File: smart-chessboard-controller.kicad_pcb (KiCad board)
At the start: 4 copper layers, 89.8 x 92.5 mm, 71 parts, among them J1 USB_C_Receptacle_USB2.0, J2 Micro_SD_Card_Det_Hirose_DM3C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, J3 Conn_02x03_Odd_Even, J4 Conn_01x12_MountingPin, J5 NX3224T024, J6 Conn_01x05, J7 Conn_01x05, J8 Conn_01x05, J9 Conn_01x05, Q1 S8050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

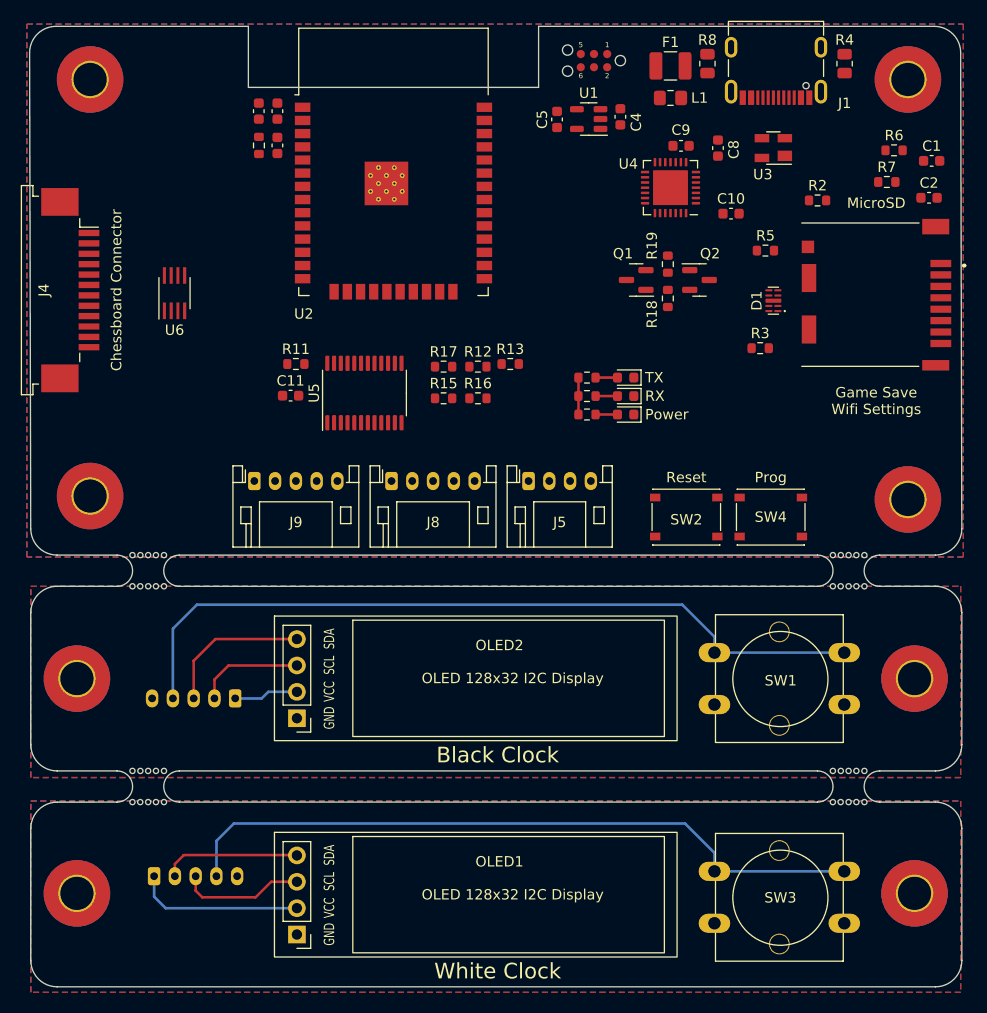
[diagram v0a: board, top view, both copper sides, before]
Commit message: change mounting hole size
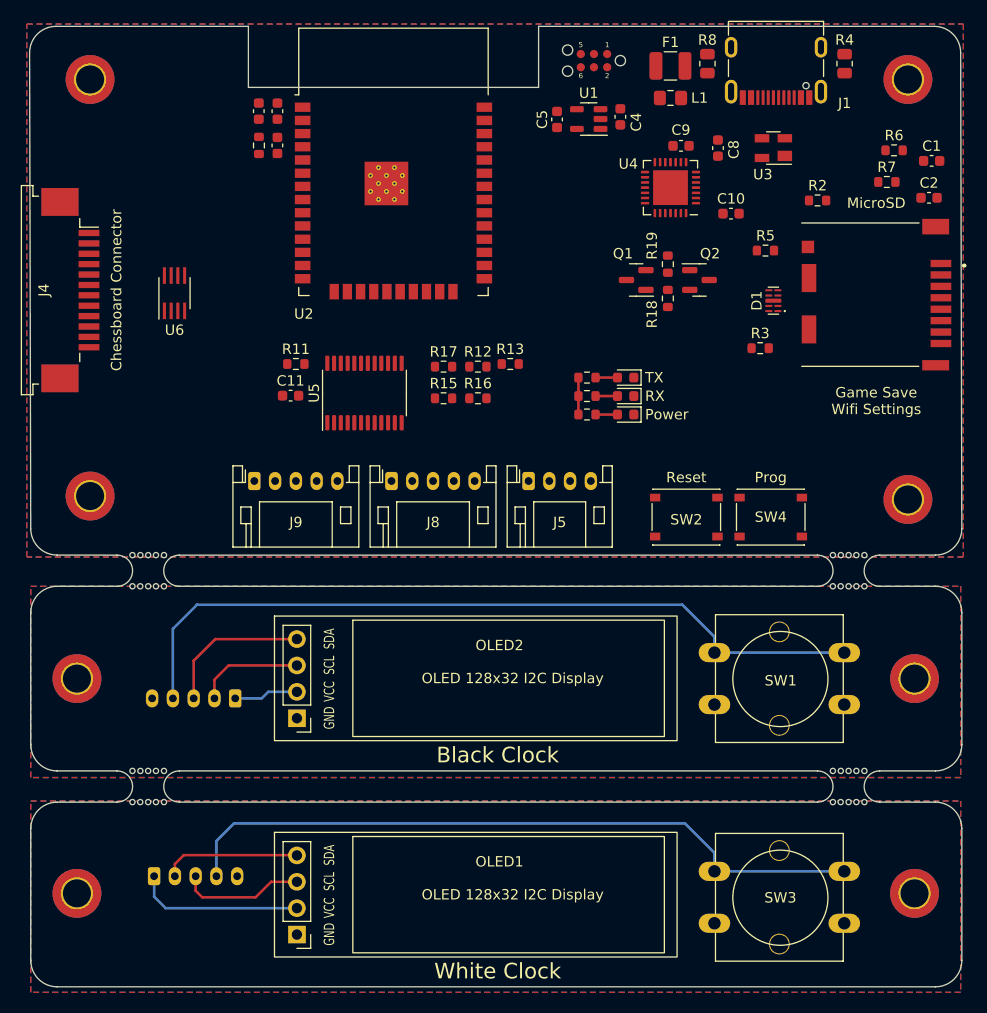
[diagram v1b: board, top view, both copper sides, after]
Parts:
- H1, H2, H3, H4, H5, H6, H7, H8: footprint MountingHole:MountingHole_3.2mm_M3_Pad_TopBottom -> MountingHole:MountingHole_2.7mm_M2.5_DIN965_Pad_TopBottom

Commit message: add some traces
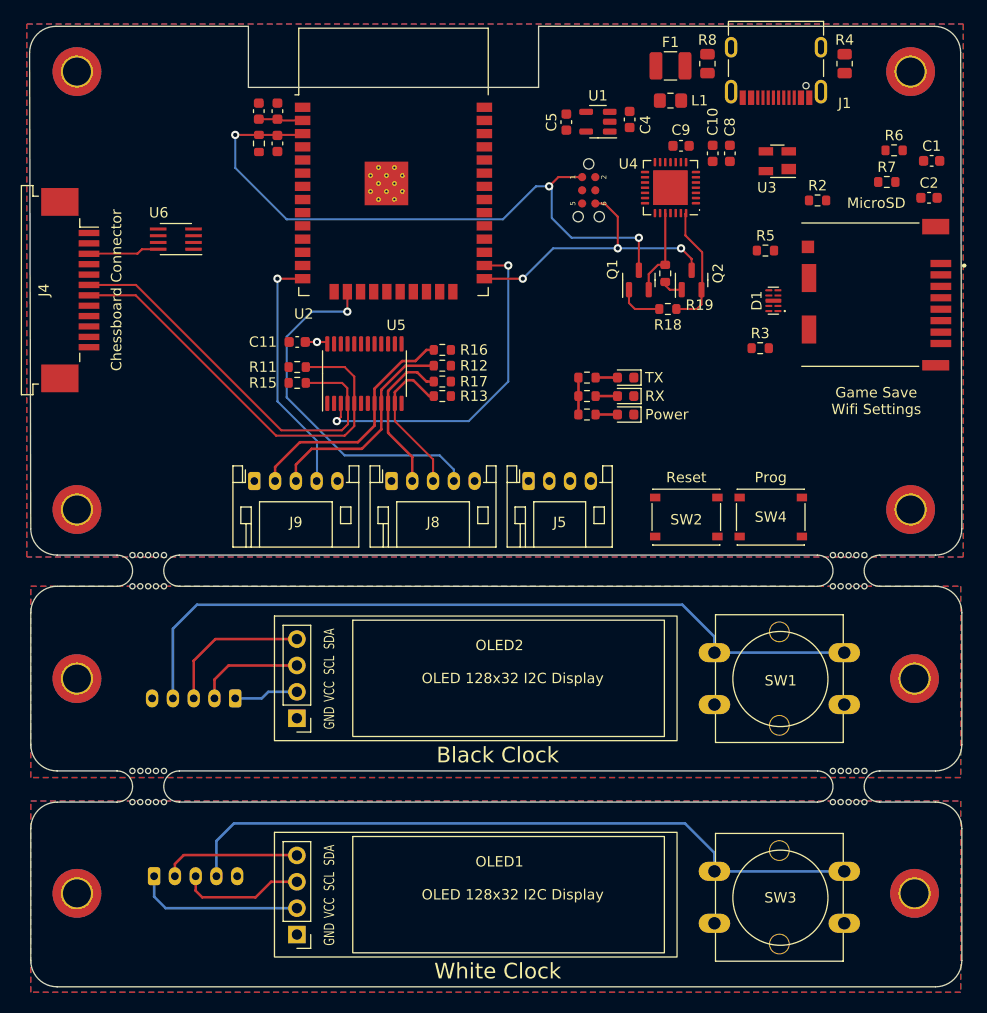
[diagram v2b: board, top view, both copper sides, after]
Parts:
- moved R15 14.2 mm to (99.4, 87.6)
- moved J3 12.5 mm to (127.5, 69.1), turned to -90 degrees
- moved R13 7.23 mm to (113.4, 88.9), turned to 180 degrees
- moved C10 6.07 mm to (139.4, 65.5), turned to 90 degrees
- moved R16 5.79 mm to (113.4, 84.5), turned to 180 degrees
- moved U6 5.21 mm to (87.8, 73.8), turned to 180 degrees
- moved C11 5.21 mm to (99.4, 83.7), turned to 180 degrees
- moved R12 3.43 mm to (113.4, 86.0), turned to 180 degrees
- moved U5 1.87 mm to (105.9, 86.7)
- moved H8 1.81 mm to (78.2, 99.8)
- moved H5 1.48 mm to (78.2, 57.7)
- moved R17 1.44 mm to (113.4, 87.5), turned to 180 degrees
- moved U3 1.33 mm to (145.7, 66.3)
- moved C8 1.25 mm to (141.1, 65.5)
- moved R18 1.02 mm to (135.1, 80.5), turned to 0 degrees
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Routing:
- net /EN: track 0.00 -> 62.7 mm, vias 0 -> 3
- net ~{SCL_IOMUX}: track 0.00 -> 41.3 mm
- net ~{SDA_IOMUX}: track 0.00 -> 38.7 mm
- net /W_MOVE: track 0.00 -> 34.7 mm, vias 0 -> 1
- net /~{I2C_RESET}: track 0.00 -> 33.4 mm, vias 0 -> 2
- net /IO0: track 0.00 -> 28.4 mm, vias 0 -> 3
- net /B_MOVE: track 0.00 -> 23.5 mm, vias 0 -> 1
- net /SCL_DBC: track 0.00 -> 23.4 mm
- net /SDA_DBC: track 0.00 -> 21.0 mm
- net /SDA_DWC: track 0.00 -> 15.1 mm
- net /SCL_DWC: track 0.00 -> 14.9 mm
- net /DTR: track 0.00 -> 12.1 mm
- net /RTS: track 0.00 -> 8.45 mm
- net /LED_IC_5: track 0.00 -> 6.84 mm
- net 3V3: track 25.9 -> 32.4 mm, vias 0 -> 1
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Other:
- board text added: "."

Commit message: add all traces and power traces
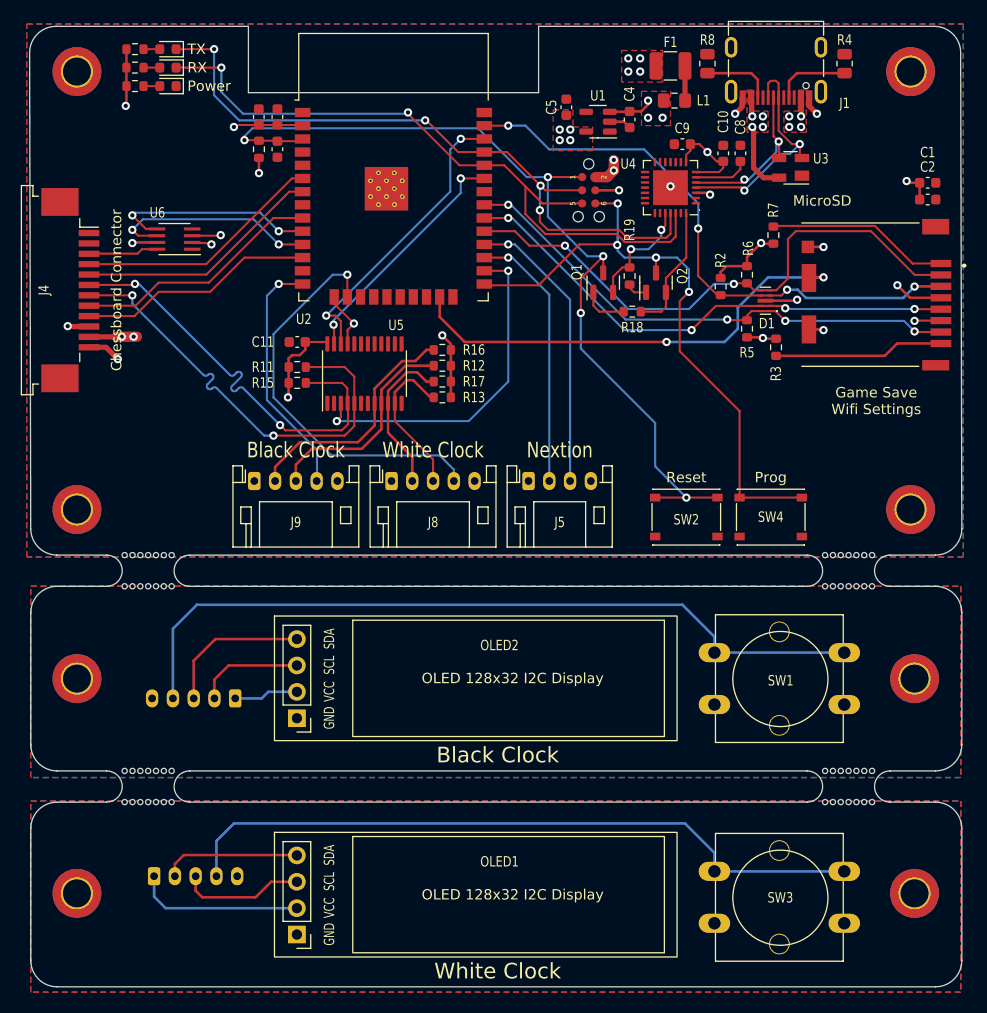
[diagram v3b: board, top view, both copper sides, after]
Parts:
- moved LED2 54.2 mm to (87.0, 57.3)
- moved LED1 54.2 mm to (87.0, 55.5)
- moved LED3 54.2 mm to (87.0, 59.1)
- moved R10 53.8 mm to (83.8, 57.3)
- moved R14 53.8 mm to (83.8, 59.1)
- moved R9 53.8 mm to (83.8, 55.5)
- moved R6 18.5 mm to (142.7, 77.2), turned to 90 degrees
- moved R2 12.5 mm to (140.2, 78.4), turned to 90 degrees
- moved R7 12.1 mm to (145.3, 73.4), turned to -90 degrees
- moved R5 7.74 mm to (142.7, 82.4), turned to -90 degrees
- moved R19 3.44 mm to (131.4, 77.3)
- moved Q1 3.44 mm to (128.9, 78.0)
- moved R18 3.44 mm to (131.7, 80.8)
- moved Q2 3.44 mm to (134.0, 78.0)
- moved C1 2.14 mm to (160.1, 68.4)
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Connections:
- U2 pad 10: /SD_SS -> /LED_IC_3
- U2 pad 11: /LED_IC_3 -> /VLS_EN
- U2 pad 29: /VLS_EN -> /SD_SS
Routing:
- net 3V3: track 32.4 -> 296.2 mm, vias 1 -> 15
- net 5V: track 0.00 -> 124.4 mm, vias 0 -> 7
- net /ESP_RX: track 0.00 -> 66.8 mm, vias 0 -> 2
- net /ESP_TX: track 0.00 -> 66.2 mm, vias 0 -> 4
- net /SD_MOSI: track 0.00 -> 55.8 mm, vias 0 -> 4
- net /SD_SS: track 0.00 -> 54.7 mm, vias 0 -> 2
- net /SD_MISO: track 0.00 -> 50.0 mm, vias 0 -> 4
- net /SD_SCK: track 0.00 -> 49.5 mm, vias 0 -> 4
- net /SD_DET: track 0.00 -> 45.1 mm, vias 0 -> 2
- net VBUS: track 0.00 -> 43.5 mm, vias 0 -> 14
- net /IO0: track 28.4 -> 61.8 mm, vias 3 -> 4
- net /~{I2C_SCL}: track 0.00 -> 28.5 mm, vias 0 -> 2
- net /TX2: track 0.00 -> 27.9 mm, vias 0 -> 1
- net GND: track 0.23 -> 27.7 mm, vias 0 -> 12
- net /RX2: track 0.00 -> 25.7 mm, vias 0 -> 1
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- added copper zone on F.Cu, net 3V3
- added copper zone on In1.Cu, net 3V3
- added copper zone on F.Cu, net 5V
- added copper zone on In1.Cu, net GND
- added copper zone on In2.Cu, net GND
- added copper zone on F.Cu, net VBUS
- added copper zone on In1.Cu, net VBUS
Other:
- outline, holes or cut-outs redrawn
- board text added: "Nextion"

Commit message: add logos and fix DRC issues
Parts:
- added REF**: KiCad-Logo2_6mm_SilkScreen, Symbol:KiCad-Logo2_6mm_SilkScreen, F.Cu at (134.1, 87.9)
- added REF**: OSHW-Logo2_9.8x8mm_SilkScreen, Symbol:OSHW-Logo2_9.8x8mm_SilkScreen, F.Cu at (85.3, 93.9)
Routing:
- net /D_N: track 16.1 -> 25.1 mm, vias 2 -> 3
- net 5V: track 124.4 -> 127.7 mm
- net 3V3: track 296.2 -> 294.9 mm
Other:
- board text added: "${COMPANY} ${TITLE} Rev ${REVISION} / ${ISSUE_DATE}"

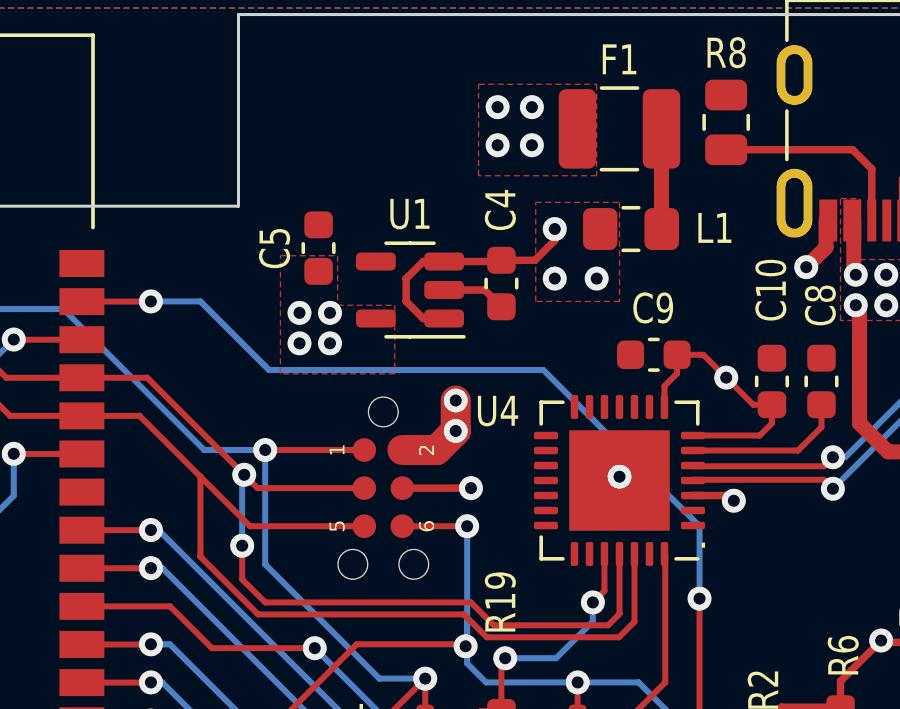
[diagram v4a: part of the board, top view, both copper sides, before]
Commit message: refactor LDO layout
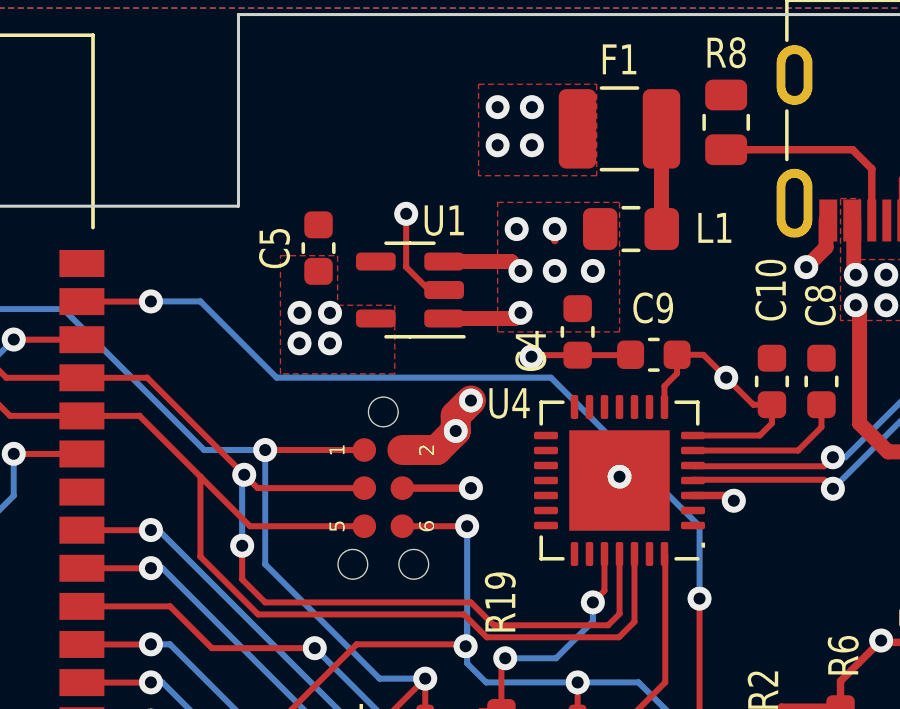
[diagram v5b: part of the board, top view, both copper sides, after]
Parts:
- moved C4 3.01 mm to (134.0, 63.9)
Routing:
- net 5V: track 127.7 -> 122.4 mm, vias 7 -> 10
- net GND: track 27.7 -> 32.2 mm, vias 12 -> 14
- added copper zone on In2.Cu, net 5V

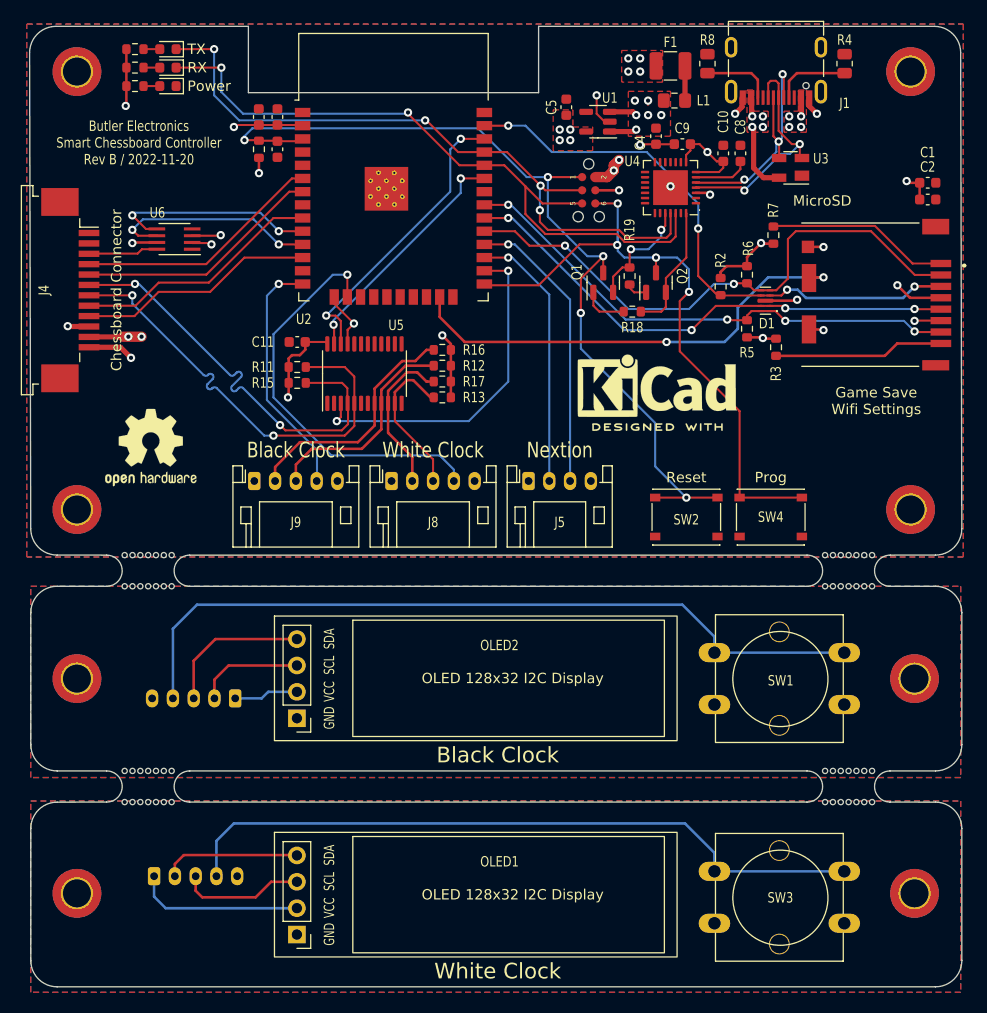
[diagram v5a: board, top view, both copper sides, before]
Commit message: move usb-c to the side of the pcb
- revise ground nets for clock boards
- add backup led IC data line if the voltage regulator fails
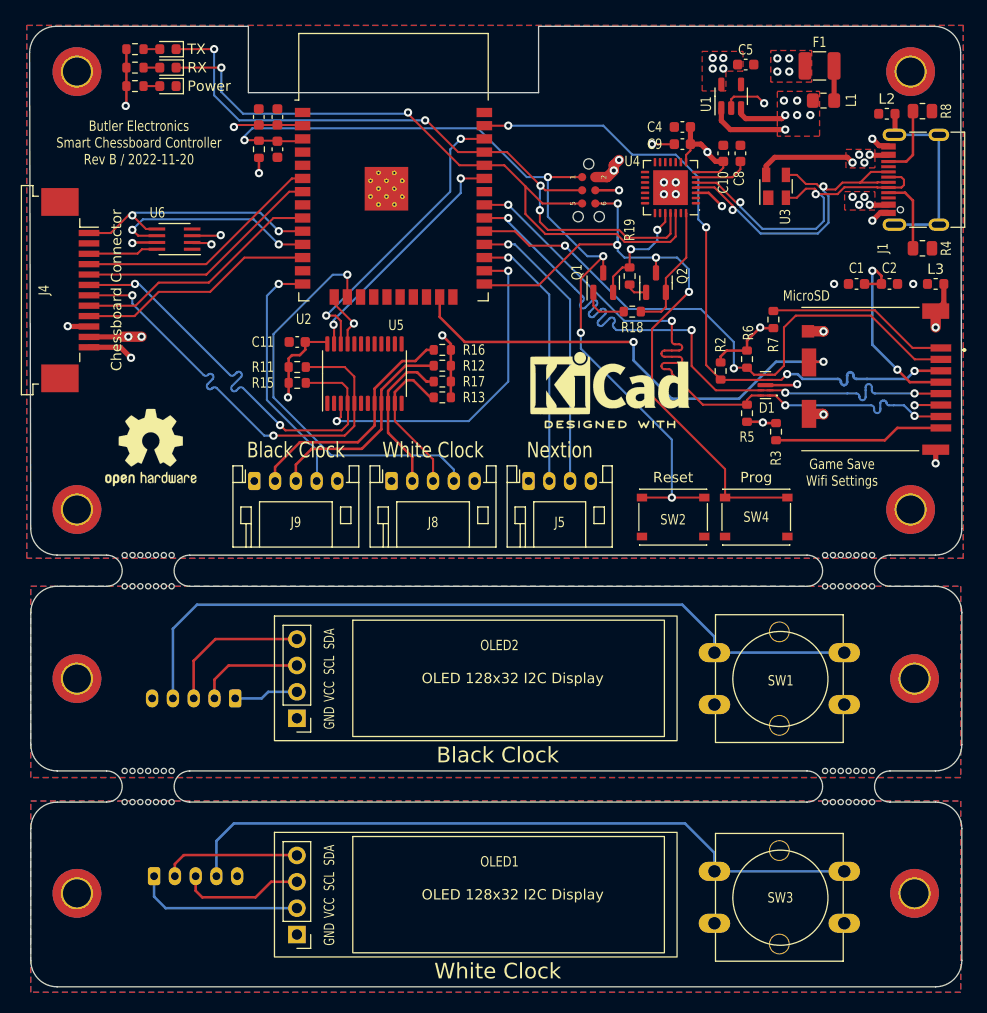
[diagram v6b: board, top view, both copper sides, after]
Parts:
- added L2: L_Ferrite_Small, Inductor_SMD:L_0603_1608Metric, F.Cu at (156.2, 61.7)
- added L3: L_Ferrite_Small, Inductor_SMD:L_0603_1608Metric, F.Cu at (160.9, 78.1)
- moved R8 21.2 mm to (159.6, 61.5), turned to 180 degrees
- moved R4 19.3 mm to (159.6, 74.7), turned to 180 degrees
- moved C5 17.8 mm to (142.6, 57.0), turned to 0 degrees
- moved J1 15.0 mm to (157.5, 68.1), turned to 90 degrees
- moved F1 14.4 mm to (149.7, 57.1)
- moved L1 14.4 mm to (150.1, 60.5)
- moved U1 13.1 mm to (141.2, 60.0), turned to 90 degrees
- moved C1 11.9 mm to (153.3, 78.1), turned to 180 degrees
- moved C2 8.92 mm to (156.5, 78.1)
- moved D1 8.13 mm to (144.5, 87.8)
- moved J2 8.13 mm to (155.1, 87.5)
- moved R2 8.13 mm to (140.2, 86.5)
- moved R3 8.13 mm to (145.5, 92.3)
- moved R5 8.13 mm to (142.7, 90.6)
- moved R6 8.13 mm to (142.7, 85.3)
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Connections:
- J1 pad S1: unconnected-(J1-PadS1) -> Net-(J1-PadS1)
- J2 pad 11: GND -> Net-(J2-Pad11)
- J4 pad 1: unconnected-(J4-Pad1) -> /LED_IC_3
- J6 pad 1: 3V3 -> +3V3
- J6 pad 5: GND -> GND1
- J7 pad 1: 3V3 -> +3.3VA
- J7 pad 5: GND -> GND2
- OLED1 pad 1: GND -> GND2
- OLED1 pad 2: 3V3 -> +3.3VA
- OLED2 pad 1: GND -> GND1
- OLED2 pad 2: 3V3 -> +3V3
- SW1 pad 2: GND -> GND1
- SW3 pad 2: GND -> GND2
- U3 pad 2: /D_P -> /D_N
- U3 pad 3: /D_N -> /D_P
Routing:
- net Net-(J2-Pad11): track 0.00 -> 41.4 mm, vias 0 -> 4
- net 3V3: track 294.9 -> 315.0 mm
- net Net-(J1-PadS1): track 0.00 -> 19.2 mm
- net +3.3VA: track 0.00 -> 16.2 mm
- net 5V: track 122.4 -> 137.6 mm
- net /SD_MISO: track 50.0 -> 64.6 mm
- net VBUS: track 43.9 -> 58.0 mm
- net /SD_SCK: track 49.5 -> 62.6 mm
- net /SD_MOSI: track 55.8 -> 66.6 mm
- net /D_P: track 23.1 -> 32.9 mm
- net /D_N: track 25.1 -> 32.6 mm, vias 3 -> 2
- net +3V3: track 0.00 -> 6.20 mm
- net /LED_IC_3: track 20.1 -> 25.0 mm
- net /SD_SS: track 54.7 -> 57.5 mm
- net /IO0: track 61.8 -> 63.5 mm
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- added copper zone on B.Cu, net GND1
- added copper zone on F.Cu, net GND1
- added copper zone on In1.Cu, net GND1
- added copper zone on In2.Cu, net GND1
- added copper zone on B.Cu, net GND2
- added copper zone on F.Cu, net GND2
- added copper zone on In1.Cu, net GND2
- added copper zone on In2.Cu, net GND2
